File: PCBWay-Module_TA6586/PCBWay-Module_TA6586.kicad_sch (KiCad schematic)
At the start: 4 parts, among them J1 Conn_01x07_Pin, J2 Conn_01x07_Pin

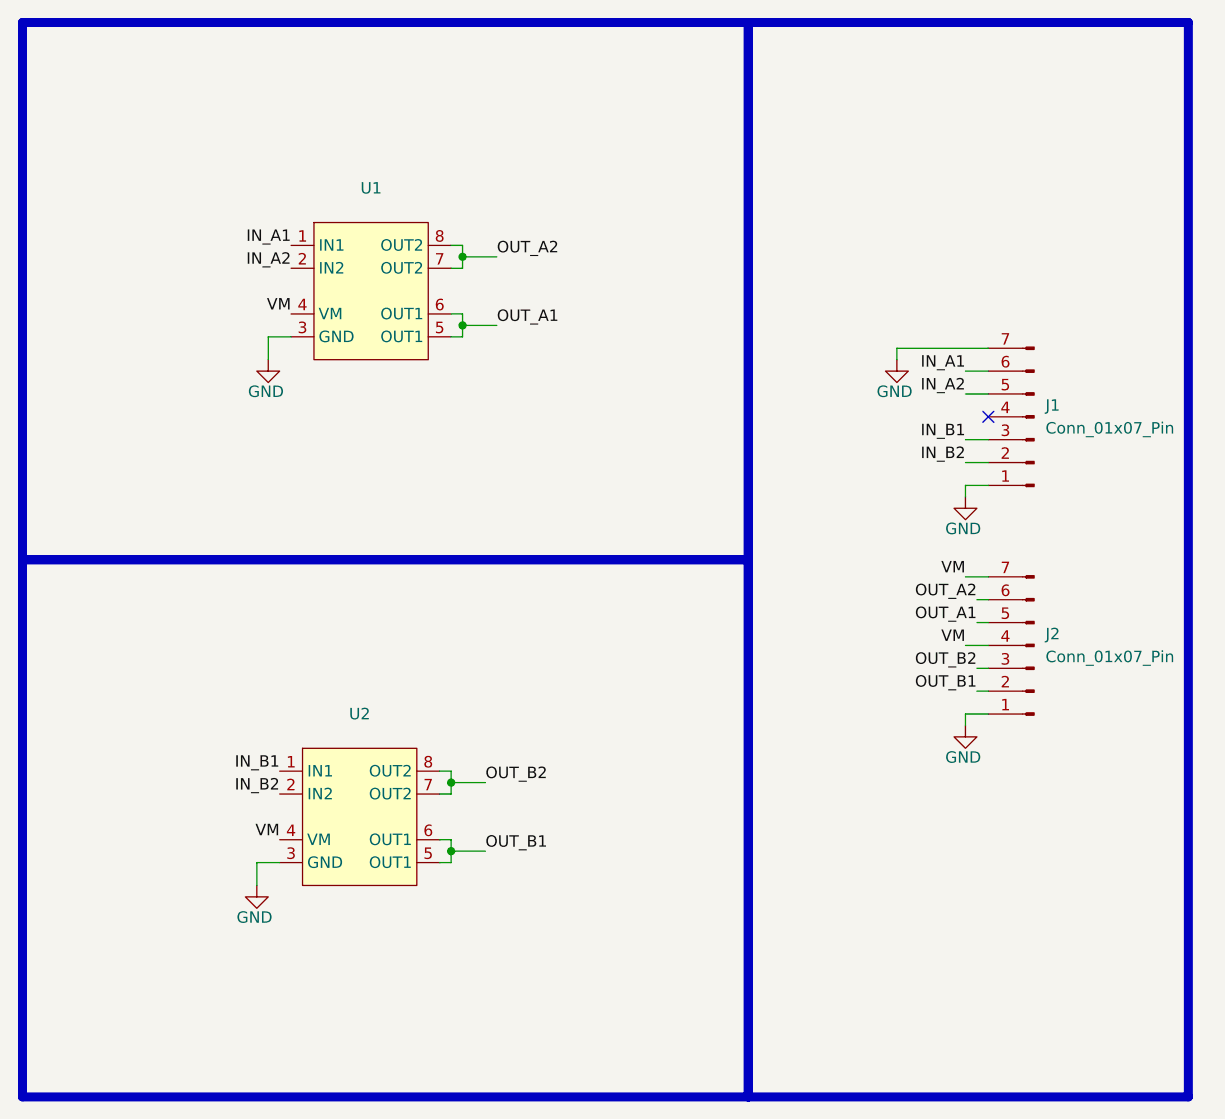
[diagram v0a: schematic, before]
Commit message: Added capacitors
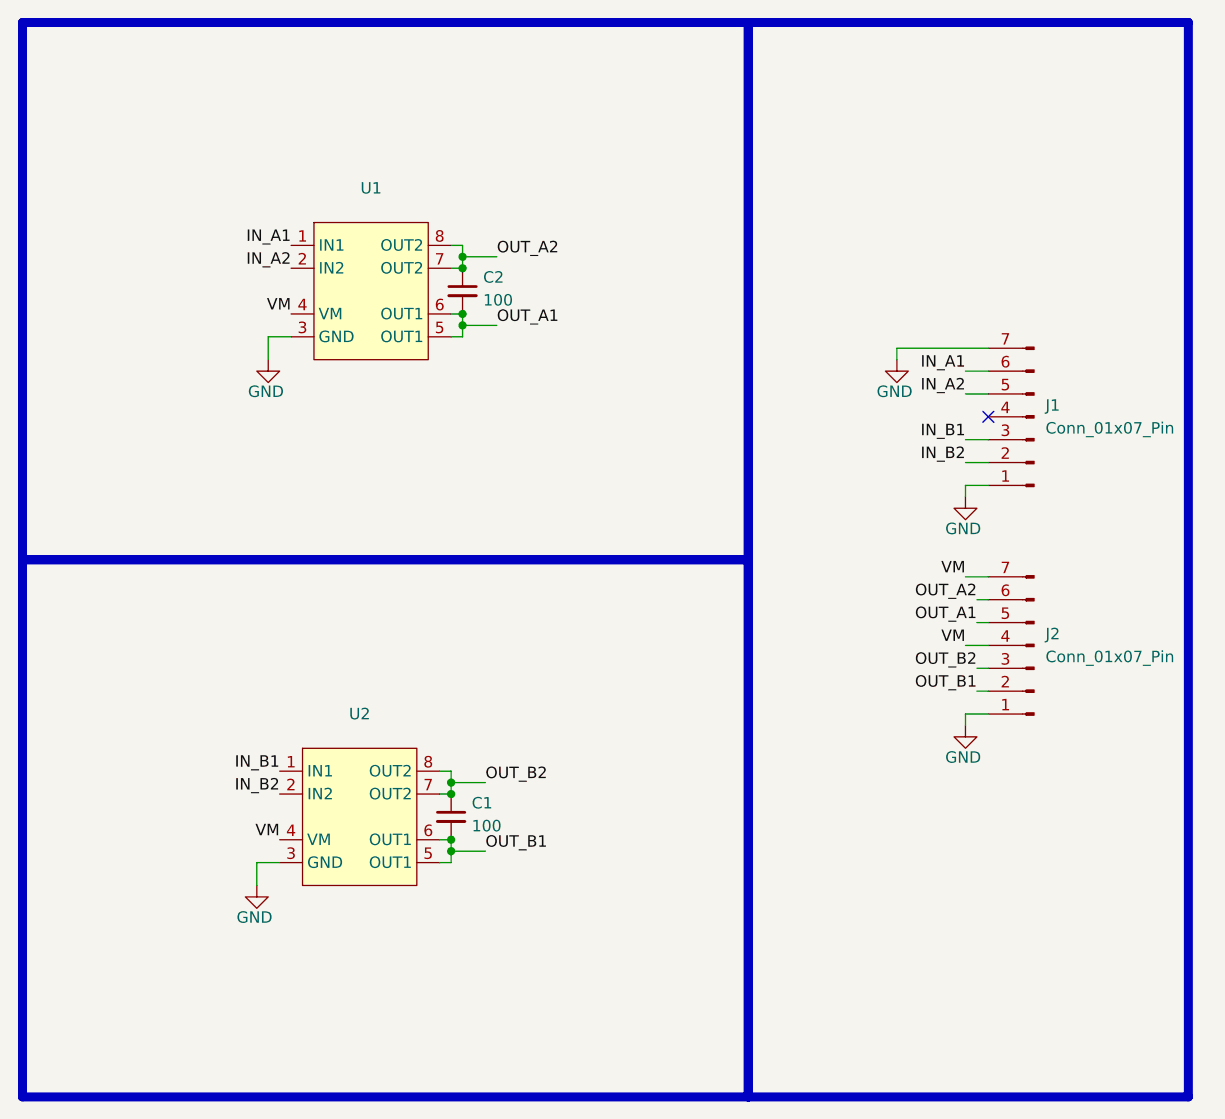
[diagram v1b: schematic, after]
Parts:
- added C1, C2: 100, Capacitor_SMD:C_0805_2012Metric, symbol Device:C_Small
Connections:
- net OUT_A1: now also C2.2
- net OUT_A2: now also C2.1
- net OUT_B1: now also C1.2
- net OUT_B2: now also C1.1
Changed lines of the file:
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@@
+	)
+	(junction
+		(at 62.23 105.41)
+		(diameter 0)
+		(color 0 0 0 0)
 	)
 	(junction
@@
 	)
 	(junction
+		(at 63.5 41.91)
+		(diameter 0)
+		(color 0 0 0 0)
+	)
+	(junction
+		(at 62.23 100.33)
+		(diameter 0)
+		(color 0 0 0 0)
+	)
+	(junction
 		(at 63.5 48.26)
 		(diameter 0)
@@
 		(color 0 0 0 0)
 	)
+	(junction
+		(at 63.5 46.99)
+		(diameter 0)
+		(color 0 0 0 0)
+	)
 	(no_connect
 		(at 121.92 58.42)
@@
 			)
 			(justify right bottom)
+		)
+	)
+	(symbol
+		(lib_id "Device:C_Small")
+		(at 62.23 102.87 0)
+		(unit 1)
+		(exclude_from_sim no)
+		(in_bom yes)
+		(on_board yes)
+		(dnp no)
+		(property "Reference" "C1"
+			(at 64.516 101.346 0)
+			(effects
+				(font
+					(size 1.27 1.27)
+				)
+				(justify left)
+			)
+		)
+		(property "Value" "100"
+			(at 64.516 103.886 0)
+			(effects
+				(font
+					(size 1.27 1.27)
+				)
+				(justify left)
+			)
+		)
+		(property "Footprint" "Capacitor_SMD:C_0805_2012Metric"
+			(at 62.23 102.87 0)
+			(effects
+				(font
+					(size 1.27 1.27)
+				)
+				(hide yes)
+			)
+		)
+		(property "Datasheet" "~"
+			(at 62.23 102.87 0)
+			(effects
+				(font
+					(size 1.27 1.27)
+				)
+				(hide yes)
+			)
+		)
+		(property "Description" "Unpolarized capacitor, small symbol"
+			(at 62.23 102.87 0)
+			(effects
+				(font
+					(size 1.27 1.27)
+				)
+				(hide yes)
+			)
+		)
+		(pin "1"
+		)
+		(pin "2"
+		)
+		(instances
+			(project "PCBWay-Module_TA6586"
+				(path "/2cdde361-a55b-48b5-9e7b-a2f6f5949c45"
+					(reference "C1")
+					(unit 1)
+				)
+			)
 		)
 	)
@@
 					(unit 1)
 				)
+			)
+		)
+	)
+	(symbol
+		(lib_id "Device:C_Small")
+		(at 63.5 44.45 0)
+		(unit 1)
+		(exclude_from_sim no)
+		(in_bom yes)
+		(on_board yes)
+		(dnp no)
+		(property "Reference" "C2"
+			(at 65.786 42.926 0)
+			(effects
+				(font
+					(size 1.27 1.27)
+				)
+				(justify left)
+			)
+		)
+		(property "Value" "100"
+			(at 65.786 45.466 0)
+			(effects
+				(font
+					(size 1.27 1.27)
+				)
+				(justify left)
+			)
+		)
+		(property "Footprint" "Capacitor_SMD:C_0805_2012Metric"
+			(at 63.5 44.45 0)
+			(effects
+				(font
+					(size 1.27 1.27)
+				)
+				(hide yes)
+			)
+		)
+		(property "Datasheet" "~"
+			(at 63.5 44.45 0)
+			(effects
+				(font
+					(size 1.27 1.27)
+				)
+				(hide yes)
+			)
+		)
+		(property "Description" "Unpolarized capacitor, small symbol"
+			(at 63.5 44.45 0)
+			(effects
+				(font
+					(size 1.27 1.27)
+				)
+				(hide yes)
+			)
+		)
+		(pin "1"
+		)
+		(pin "2"
+		)
+		(instances
+			(project "PCBWay-Module_TA6586"
+				(path "/2cdde361-a55b-48b5-9e7b-a2f6f5949c45"
+					(reference "C2")
+					(unit 1)
+				)

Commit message: Modified capacitors value
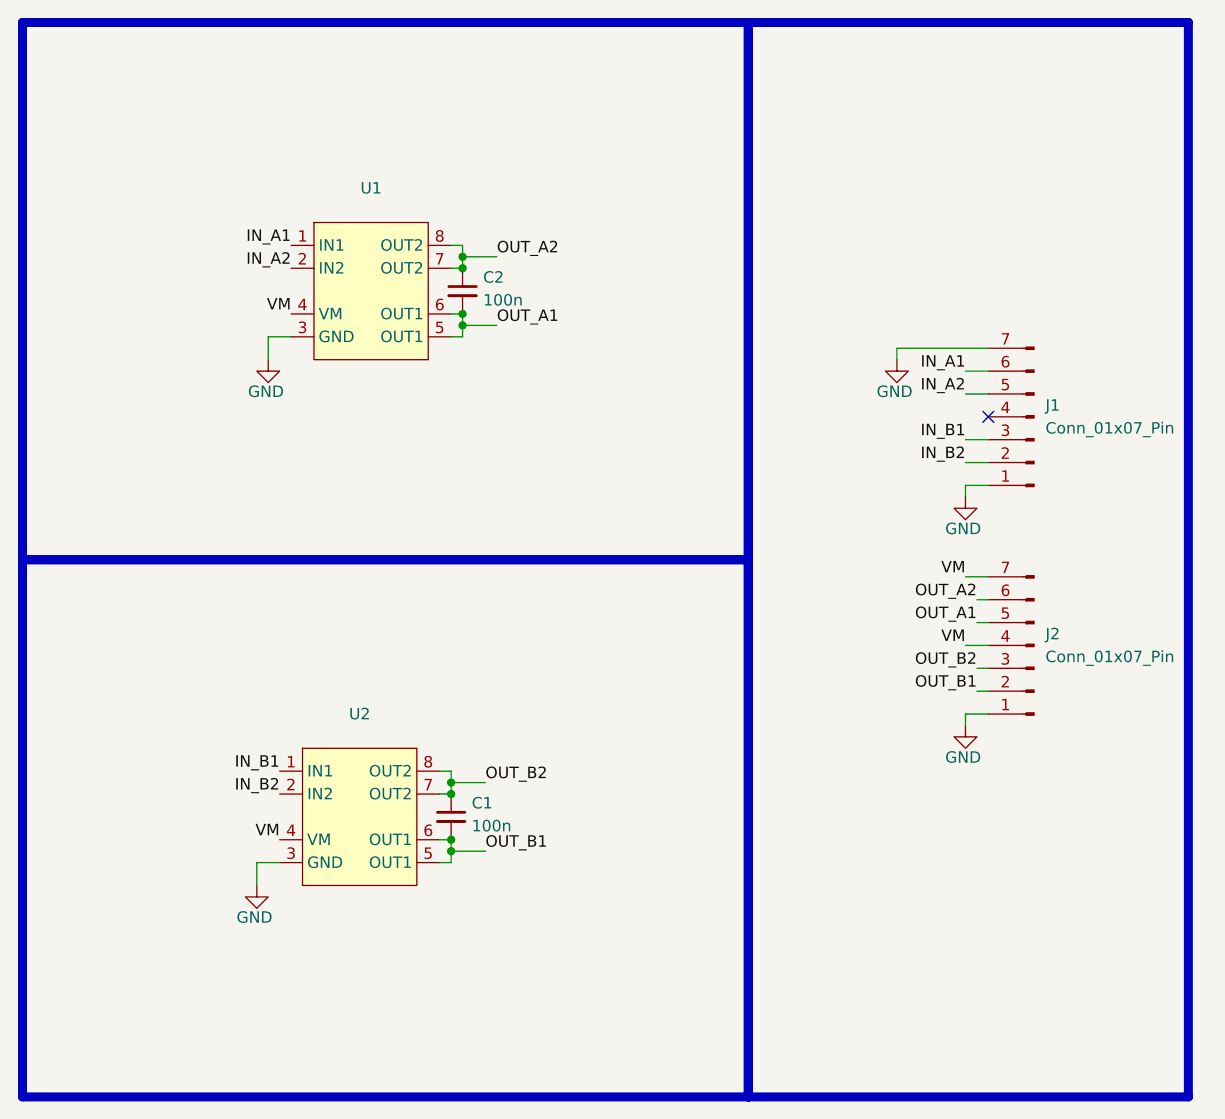
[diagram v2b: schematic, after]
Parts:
- C1, C2: value 100 -> 100n
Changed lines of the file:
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@@
 			)
 		)
-		(property "Value" "100"
+		(property "Value" "100n"
 			(at 64.516 103.886 0)
 			(effects
@@
 			)
 		)
-		(property "Value" "100"
+		(property "Value" "100n"
 			(at 65.786 45.466 0)
 			(effects
